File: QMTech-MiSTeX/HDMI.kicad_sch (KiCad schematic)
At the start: 38 parts, among them U3 TPS76318, U4 ADV7513BSWZ

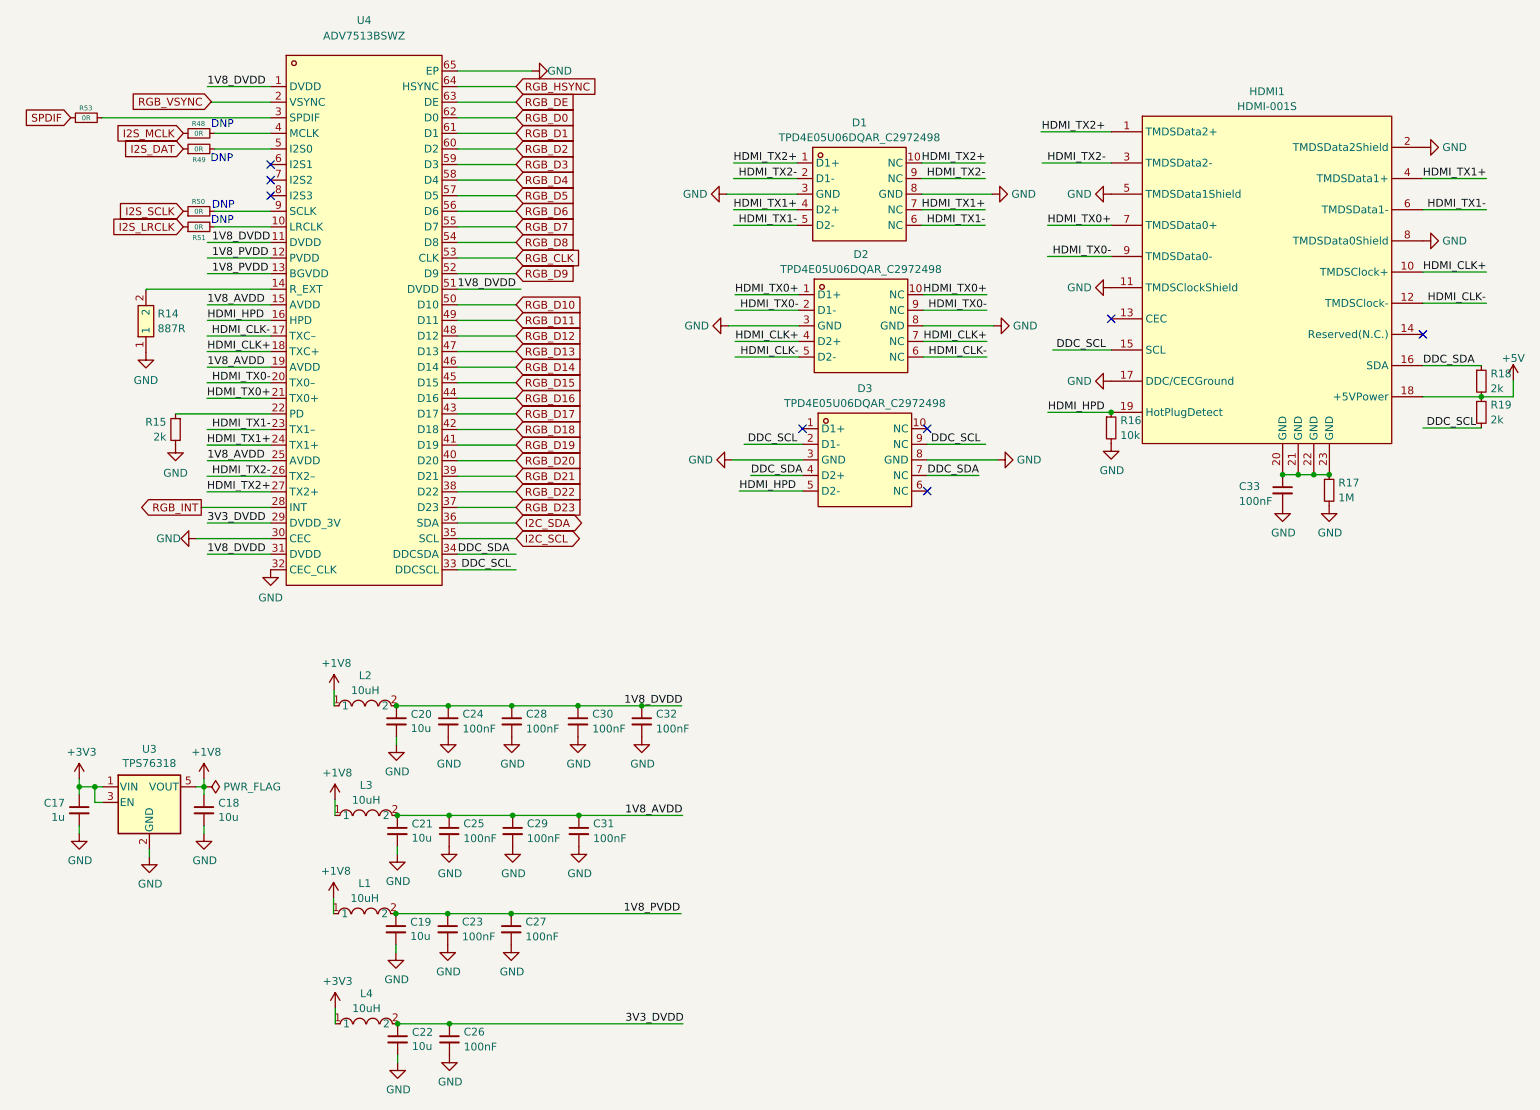
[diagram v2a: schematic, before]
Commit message: finish routing/layouting, fix silk screen, add mounting holes
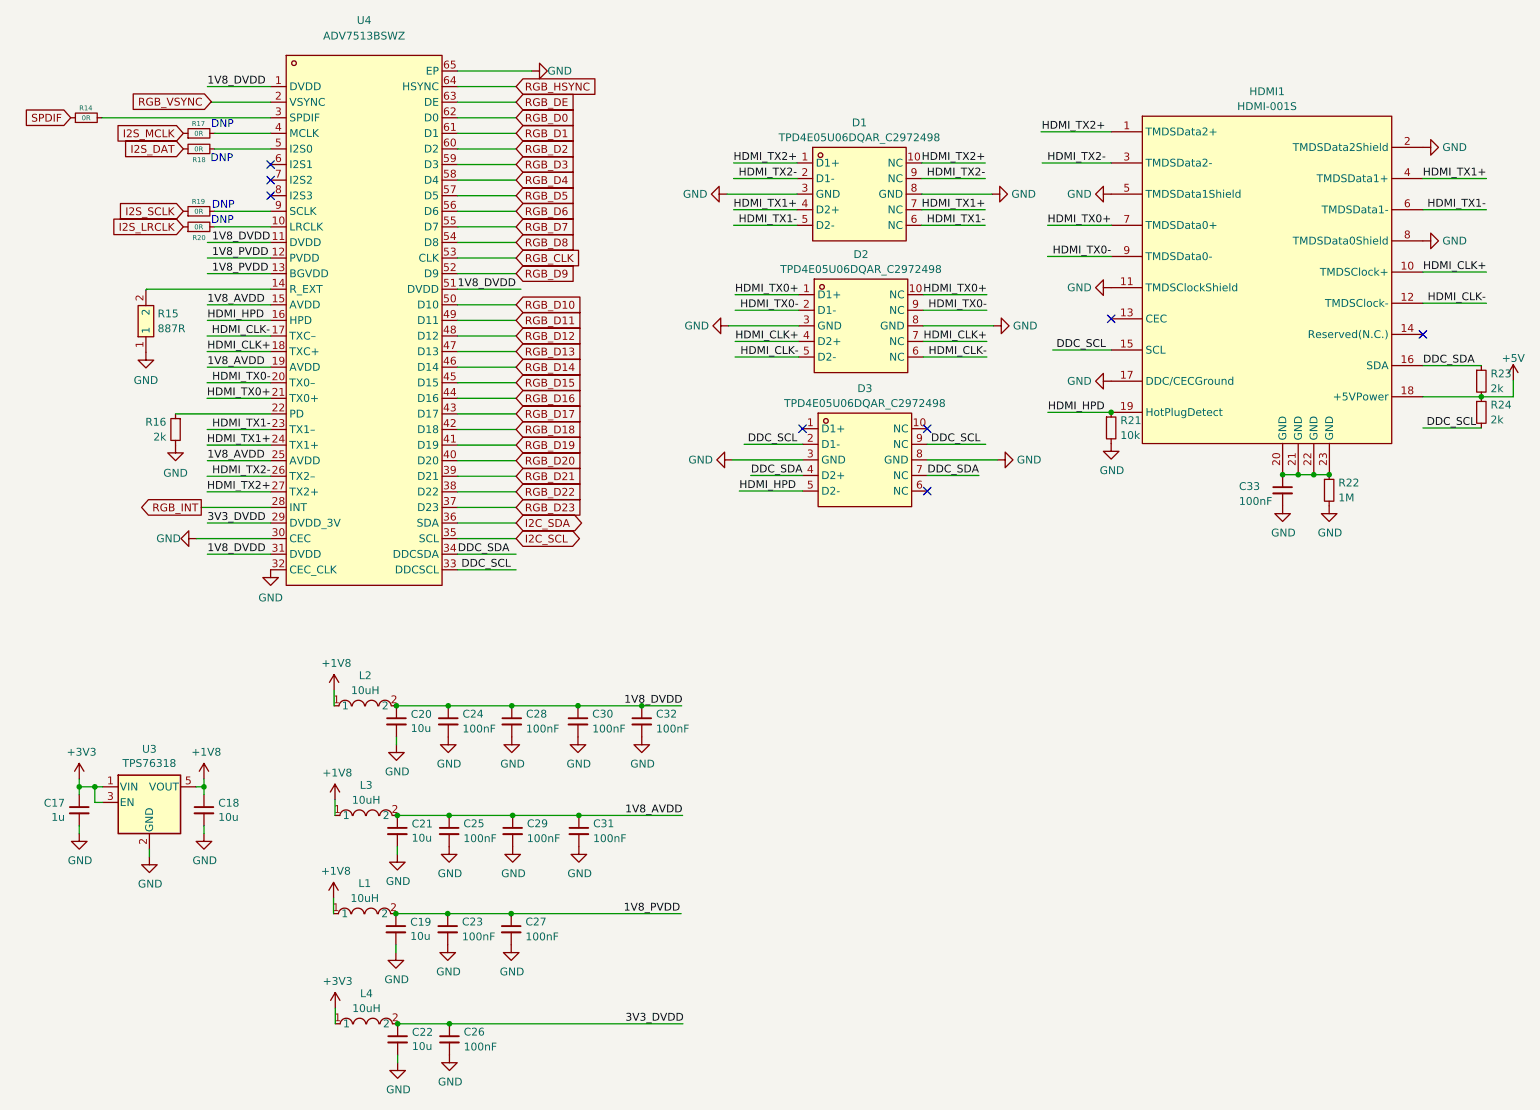
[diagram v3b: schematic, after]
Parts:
- renumbered R53 to R14, R14 to R15, R15 to R16, R48 to R17, R49 to R18, R50 to R19, R51 to R20, R16 to R21, R17 to R22, R18 to R23, R19 to R24

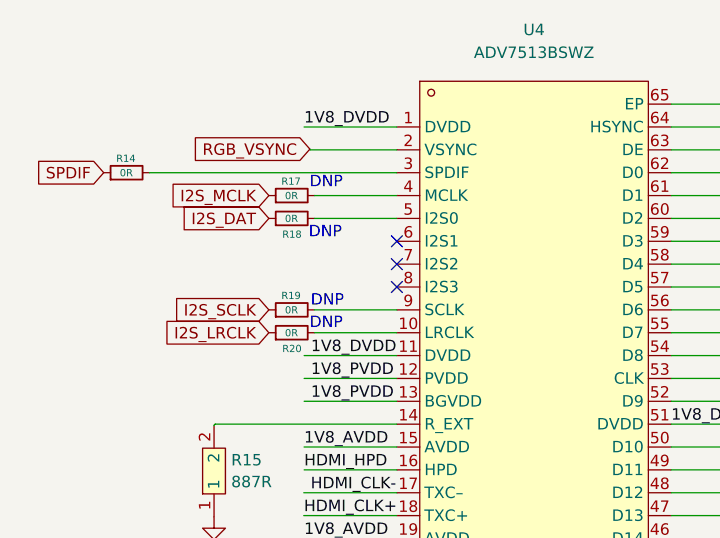
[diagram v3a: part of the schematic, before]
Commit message: fix DRC errors and some warnings too
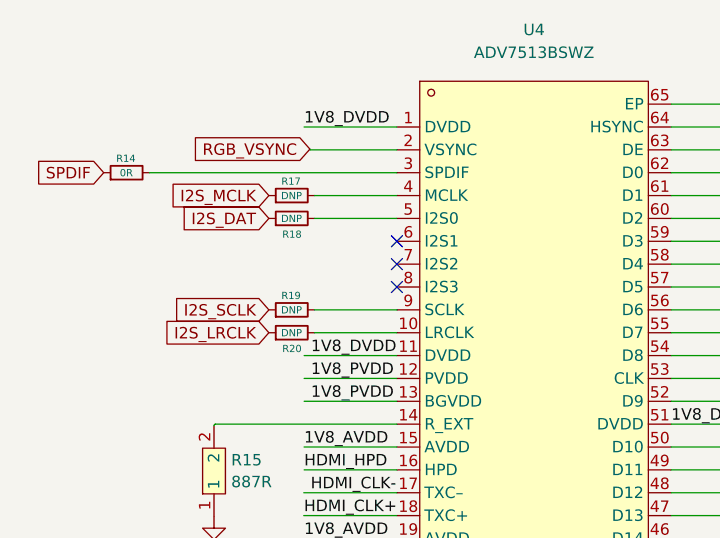
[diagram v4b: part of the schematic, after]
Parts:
- R17, R18, R19, R20: value 0R -> DNP
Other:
- note removed: "DNP"
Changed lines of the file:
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@@
     )
-  )
-  (text "DNP" (at 49.5046 39.4716 0)
-    (effects (font (size 1.27 1.27)) (justify left bottom))
-  )
-  (text "DNP" (at 49.6062 49.5554 0)
-    (effects (font (size 1.27 1.27)) (justify left bottom))
-  )
-  (text "DNP" (at 49.6062 33.909 0)
-    (effects (font (size 1.27 1.27)) (justify left bottom))
-  )
-  (text "DNP" (at 49.7332 47.0662 0)
-    (effects (font (size 1.27 1.27)) (justify left bottom))
   )
   (label "DDC_SCL" (at 195.426 69.85 180) (fields_autoplaced)
@@
       (effects (font (size 0.8 0.8)))
     )
-    (property "Value" "0R" (at 47.5996 37.1094 90)
+    (property "Value" "DNP" (at 47.5996 37.1094 90)
       (effects (font (size 0.8 0.8)))
     )
@@
       (effects (font (size 0.8 0.8)))
     )
-    (property "Value" "0R" (at 47.5996 34.5694 90)
+    (property "Value" "DNP" (at 47.5996 34.5694 90)
       (effects (font (size 0.8 0.8)))
     )
@@
       (effects (font (size 0.8 0.8)))
     )
-    (property "Value" "0R" (at 47.5996 49.8094 90)
+    (property "Value" "DNP" (at 47.5996 49.8094 90)
       (effects (font (size 0.8 0.8)))
     )
@@
       (effects (font (size 0.8 0.8)))
     )
-    (property "Value" "0R" (at 47.5996 47.2694 90)
+    (property "Value" "DNP" (at 47.5996 47.2694 90)
       (effects (font (size 0.8 0.8)))
     )

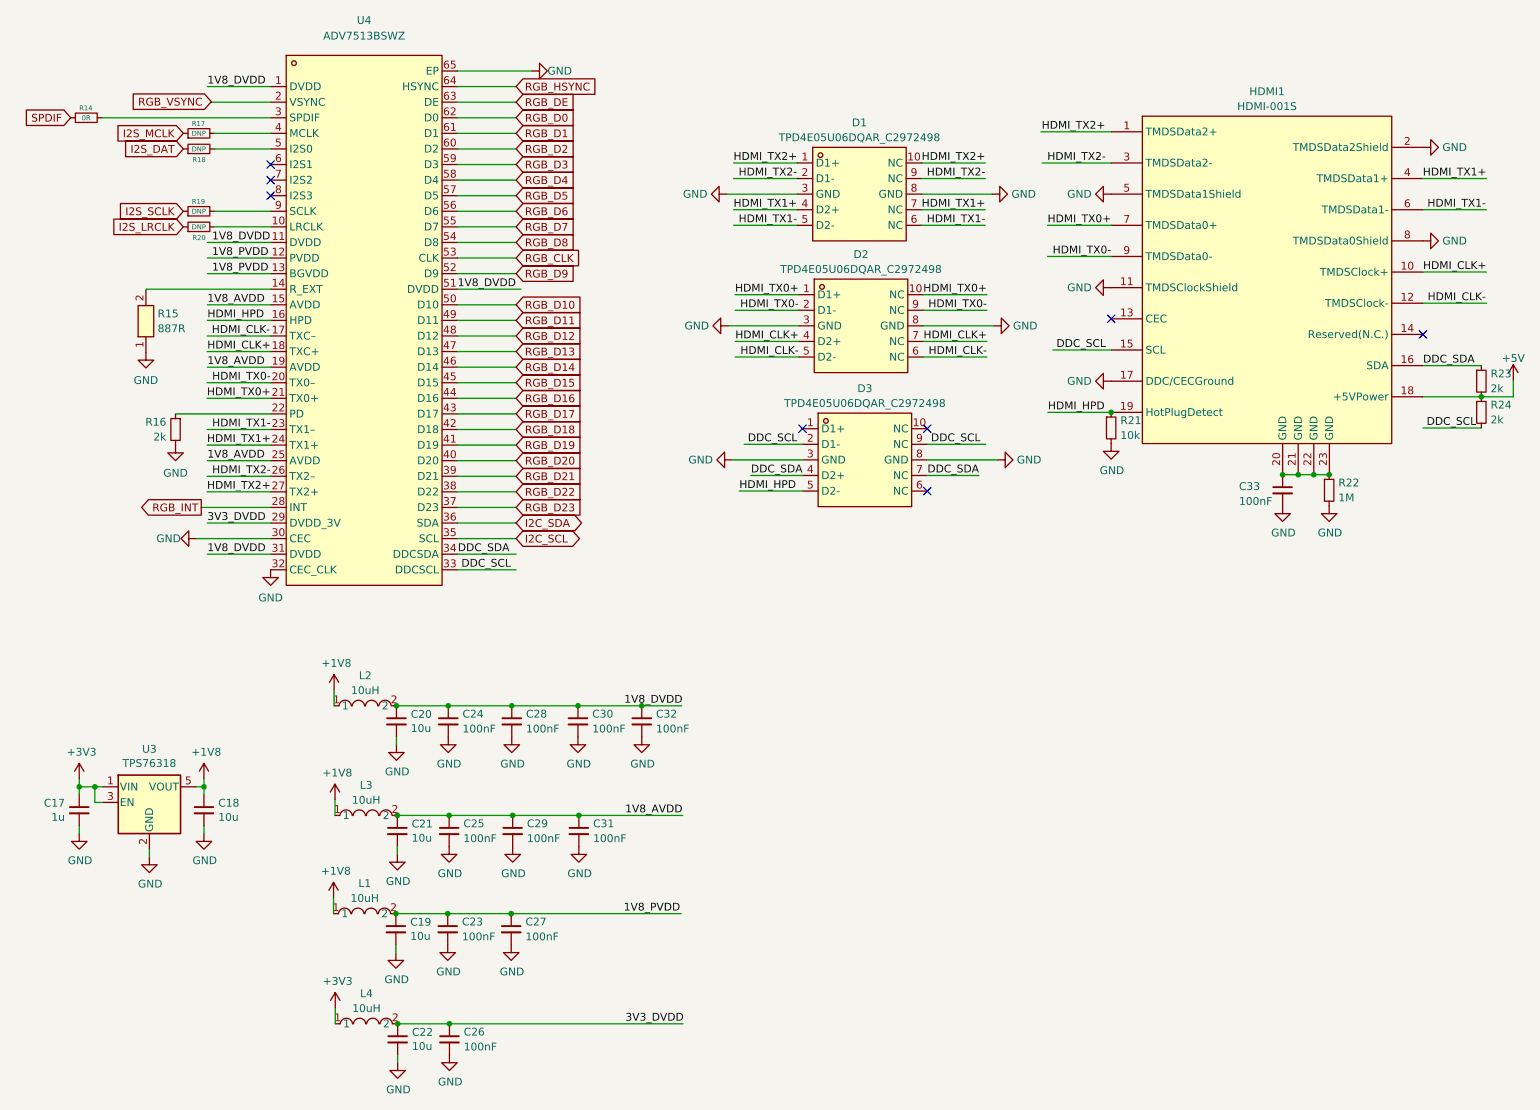
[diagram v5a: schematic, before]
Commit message: power filtering, testpoints, bottom caps, more decoupling, teardrops
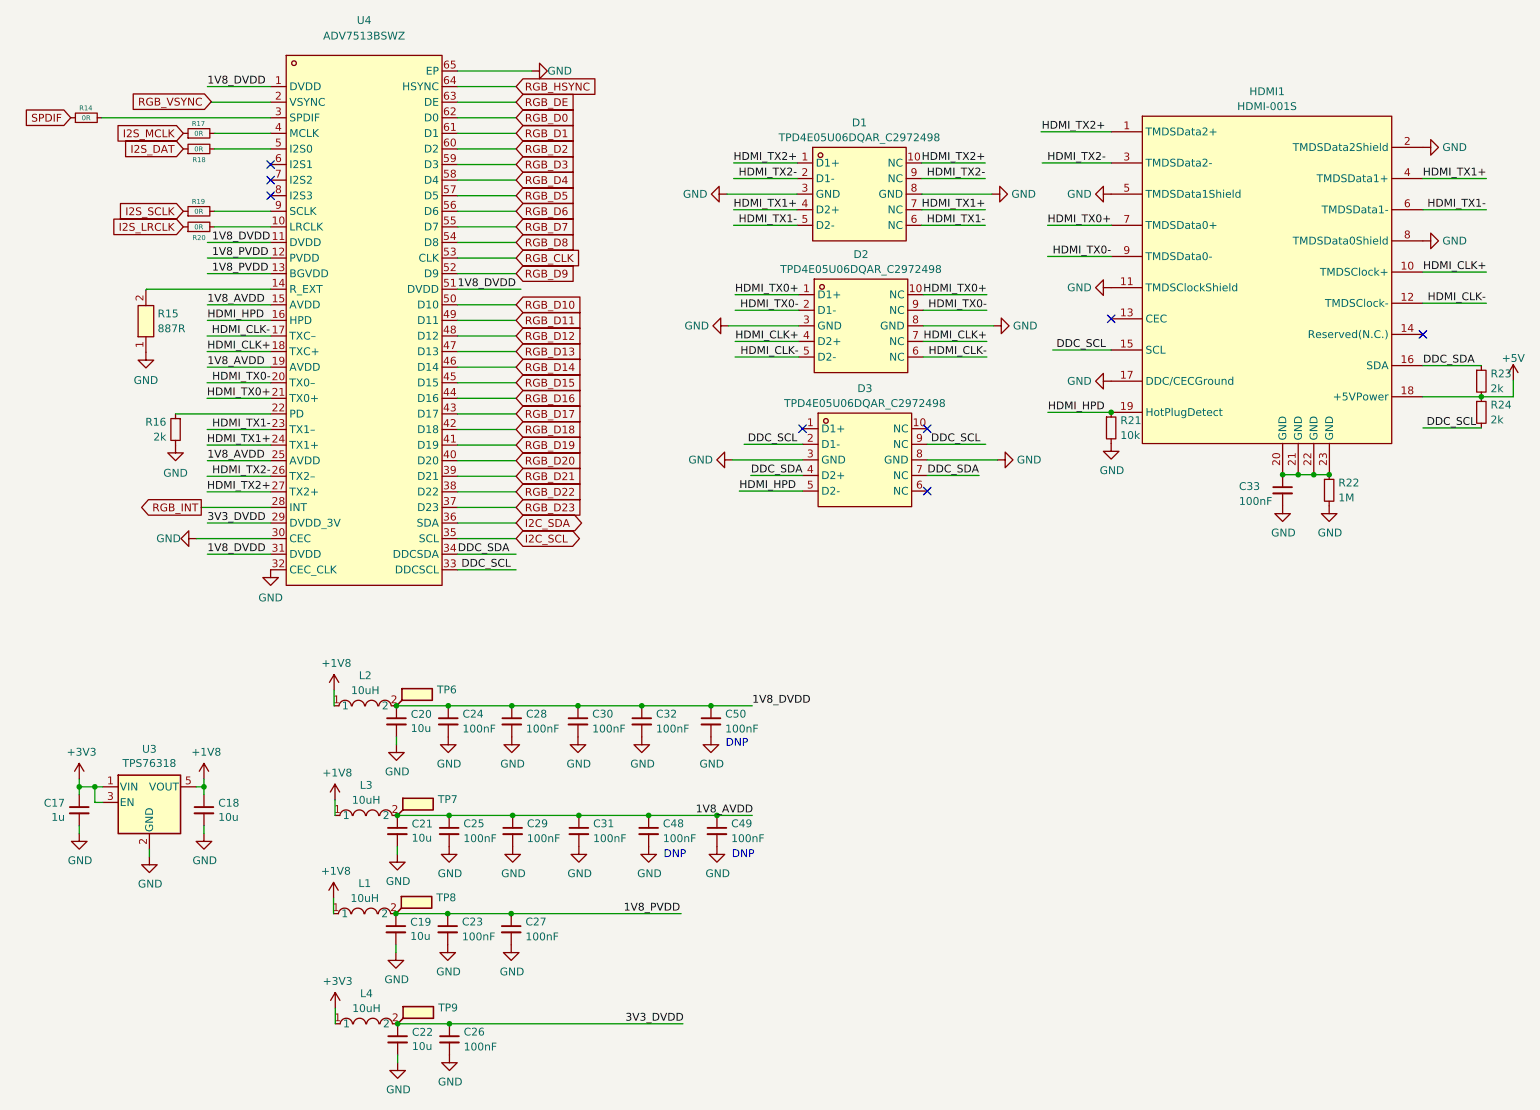
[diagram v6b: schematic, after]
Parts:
- added C48, C49, C50: 100nF, C_0805_2012Metric, symbol jlcpcb-basic-mlcc-0805:100nF
- added TP6, TP7, TP8, TP9: TestPoint_Flag, TestPoint:TestPoint_Pad_D1.5mm, symbol Connector:TestPoint_Flag
- R17, R18, R19, R20: value DNP -> 0R; LCSC (none) -> C17168
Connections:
- net 1V8_AVDD: now also C48.1, C49.1, TP7.1
- net 1V8_DVDD: now also C50.1, TP6.1
- net 1V8_PVDD: now also TP8.1
- net 3V3_DVDD: now also TP9.1
- net GND: now also C48.2, C49.2, C50.2
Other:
- note added: "DNP"
- title: (none) -> HDMI Video Output
